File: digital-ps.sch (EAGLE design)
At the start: 74 parts, among them CON1 SWD_CON, IC1 STM32F334K8, IC2 MCP14700, IC3 7805, IC4 7805, IC5 S812, Q1 40V, Q2 40V

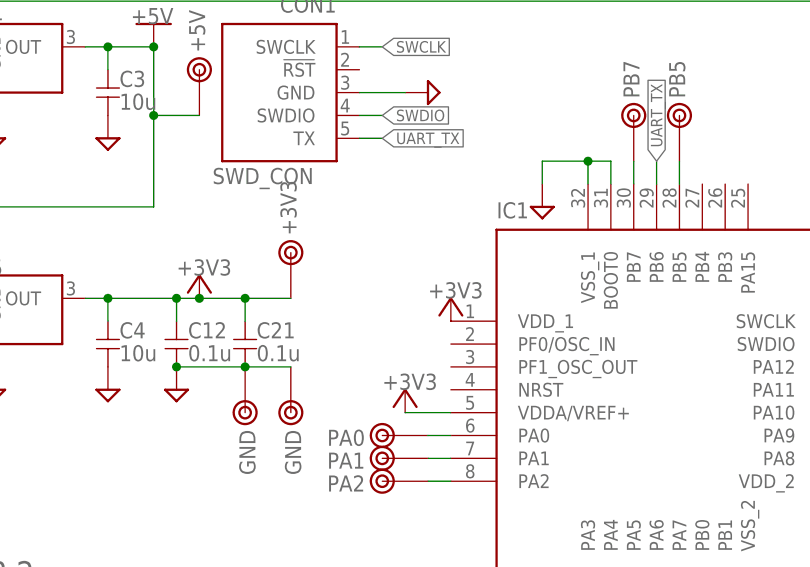
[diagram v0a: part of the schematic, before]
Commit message: FETのゲート逆だった
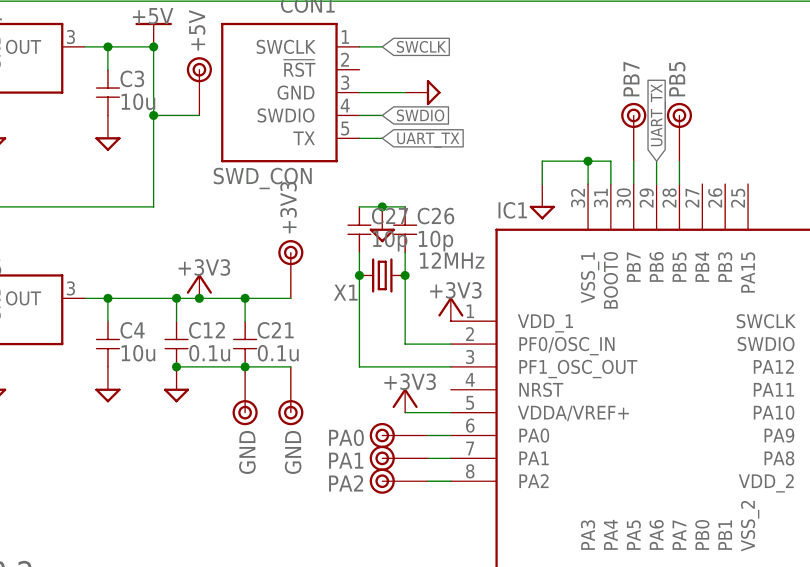
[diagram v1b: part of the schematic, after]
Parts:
- added C26, C27: 10p, my_rcl:C-1608
- added X1: 12MHz, my_rcl:CRYSTALHC49S
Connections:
- new net N$24: C26.2, IC1.PF0/OSC_IN, X1.1
- new net N$25: C27.2, IC1.PF1_OSC_OUT, X1.2
- net GND: now also C26.1, C27.1

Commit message: F303 GaN FET
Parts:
- removed TP14: PA10, my_connector:TESTPIN
- added C28: 0.1u, my_rcl:C-1608
- added R16, R4: 10k, my_rcl:R-2012
- added TP21: PA15, my_connector:TESTPIN
- added TP22: PB3, my_connector:TESTPIN
- added TP23: PB4, my_connector:TESTPIN
- C6: value 10u -> 1u; device my_rcl:C-3216 -> my_rcl:C-2012
- IC1: value STM32F334K8 -> STM32F303K8T6; device my_ic:STM32F334K8 -> my_ic:STM32F303K8T6
- IC5: value S812 -> 3.3V; device my_ic:S812 -> my_ic:78X-SOP
- Q1: value 40V -> EPC2052; device my_ic:NMOS-DFN -> my_ic:NMOSEPC2052
- Q2: value 40V -> (none); device my_ic:NMOS-DFN -> my_ic:NMOSEPC2052
- R7: value 100m -> 40m
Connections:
- removed net N$2: IC1.PA9, R5.1
- new net N$23: IC1.PB4, TP23.1
- new net N$26: IC1.PB3, TP22.1
- new net N$27: IC1.PA15, TP21.1
- net +3V3: now also C28.1
- net GND: now also C28.2, R16.1
- net N$10: now also R16.2
- net N$20: now also R5.1; no longer TP14.1
- net N$9: now also R4.2
- net OUT+: no longer C9.1
- net SW: now also R4.1
- net SWCLK: now also IC1.PA14; no longer IC1.SWCLK
- net SWDIO: now also IC1.PA13; no longer IC1.SWDIO
- net VP: now also C9.1
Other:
- moved on the sheet: C5, C6, C7, C8, C9, R5

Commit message: 発注
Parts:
- added C29: 1n, my_rcl:C-1608
- added R17: 10, my_rcl:R-2012
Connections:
- new net N$2: C29.1, R17.1
- net GND: now also C29.2
- net SW: now also R17.2
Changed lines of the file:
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@@
 <part name="R16" library="my_rcl" deviceset="R" device="-2012" value="10k"/>
 <part name="SUPPLY32" library="my_supply" deviceset="GND" device=""/>
+<part name="R17" library="my_rcl" deviceset="R" device="-2012" value="10"/>
+<part name="C29" library="my_rcl" deviceset="C" device="-1608" value="1n"/>
+<part name="SUPPLY33" library="my_supply" deviceset="GND" device=""/>
 </parts>
 <sheets>
@@
 </instance>
 <instance part="SUPPLY32" gate="GND" x="154.94" y="20.32" smashed="yes"/>
+<instance part="R17" gate="G$1" x="172.72" y="38.1" smashed="yes" rot="R90">
+<attribute name="NAME" x="171.2214" y="34.29" size="1.778" layer="95" rot="R90"/>
+<attribute name="VALUE" x="176.022" y="34.29" size="1.778" layer="96" rot="R90"/>
+</instance>
+<instance part="C29" gate="G$1" x="172.72" y="30.48" smashed="yes">
+<attribute name="NAME" x="173.99" y="31.115" size="1.778" layer="95"/>
+<attribute name="VALUE" x="173.99" y="28.575" size="1.778" layer="96"/>
+</instance>
+<instance part="SUPPLY33" gate="GND" x="172.72" y="25.4" smashed="yes"/>
 </instances>
 <busses>
@@
 <pinref part="R16" gate="G$1" pin="1"/>
 <pinref part="SUPPLY32" gate="GND" pin="GND"/>
+</segment>
+<segment>
+<pinref part="C29" gate="G$1" pin="2"/>
+<pinref part="SUPPLY33" gate="GND" pin="GND"/>
 </segment>
 </net>
@@
 <junction x="137.16" y="40.64"/>
 <pinref part="L1" gate="G$1" pin="1"/>
-<wire x1="175.26" y1="45.72" x2="165.1" y2="45.72" width="0.1524" layer="91"/>
+<wire x1="175.26" y1="45.72" x2="172.72" y2="45.72" width="0.1524" layer="91"/>
 <junction x="165.1" y="45.72"/>
 <label x="170.18" y="45.72" size="1.778" layer="95"/>
 <pinref part="R4" gate="G$1" pin="1"/>
 <junction x="154.94" y="40.64"/>
+<pinref part="R17" gate="G$1" pin="2"/>
+<wire x1="172.72" y1="45.72" x2="165.1" y2="45.72" width="0.1524" layer="91"/>
+<wire x1="172.72" y1="43.18" x2="172.72" y2="45.72" width="0.1524" layer="91"/>
+<junction x="172.72" y="45.72"/>
 </segment>
 </net>
@@
 </segment>
 </net>
+<net name="N$2" class="0">
+<segment>
+<pinref part="R17" gate="G$1" pin="1"/>
+<pinref part="C29" gate="G$1" pin="1"/>
+</segment>
+</net>
